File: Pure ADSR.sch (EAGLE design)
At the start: 42 parts, among them Q1 20MHz, U1 ATMEGA328P

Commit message: ADSR 2.1
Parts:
- removed BUT: PB6149L-5, INSTRUO:PB6149L-5
- removed IN, OUT: S_JACK, INSTRUO:S_JACK
- removed JP1: M05X2SHD, SparkFun-Connectors:M05X2SHD
- removed MODE: TOGGLE_ON_OFF_ON, INSTRUO:TOGGLE_ON_OFF_ON
- removed POT_A, POT_D, POT_R, POT_S: Q-POT, INSTRUO:Q-POT
- removed U$1: 2N3904, INSTRUO:TRANSISTOR_MMBT3904
- removed U$2: MCP4921, INSTRUO:MCP4921
- removed U$3: DUAL_OPAMP, INSTRUO:DUAL_OPAMP
- removed U$4: 7805, INSTRUO:V-REG
- removed U1: ATMEGA328P, SparkFun-DigitalIC:ATMEGA328_SMT
- added ATTACK, DECAY, RELEASE, SUSTAIN: 100k, GMSN:RESISTOR_VARIABLE9MM_POT
- added IC1: 78M05, GMSN:VOLTAGE_REG_POS05DT
- added IC2: OPAMP_DUALD, GMSN:OPAMP_DUALD
- added IC3: MCP4921, GMSN:DAC_SINGLE_12B_MCP4921
- added IC4: ATMEGA328P, GMSN:MICROPROCESSOR_ATMEGA328_SMT
- added MODESW: ON_OFF_ON, GMSN:SWITCH_TOGGLE_ON_OFF_ON
- added OUTPUT, TRIGATEIN: SOCKET_MONO_3.5MMPJ301M-12, GMSN:SOCKET_MONO_3.5MMPJ301M-12
- added POWER: HEADER2X5SHD, GMSN:HEADER2X5SHD
- added T1: MMBT2222A, GMSN:TRANSISTOR_NPNMMBT2222A
- added TRIGGER: PB6149L-5, GMSN:SWITCH_PUSHBUTTON_LED
- C1, C2, C6: device rcl:C-USC0805K -> GMSN:CAPACITOR-USC0805
- C10, C11, C12, C8, C9: value 0.1u -> 100nF; device rcl:C-USC0805K -> GMSN:CAPACITOR-USC0805
- C3: value 560p -> 10nF; device rcl:C-USC0805K -> GMSN:CAPACITOR-USC0805
- C4, C5, C7: device rcl:CPOL-US153CLV-0505 -> GMSN:CAPACITOR_POL-US153CLV-0505
- D1, D2: value (none) -> STTH102A; device adafruit:DIODESMA -> GMSN:DIODESMA
- ISP1: value AVRISP-6 -> HEADER2X3-6; device adafruit:AVRISP-6 -> GMSN:HEADER2X3-6
- Q1: device adafruit:CRYSTALHC49UP -> GMSN:CRYSTALHC49UP
- R1: value 47K -> 56k; device rcl:R-US_R0805 -> GMSN:RESISTOR_USR0805
- R10, R8: value 1K -> 1k; device rcl:R-US_R0805 -> GMSN:RESISTOR_USR0805
- R11, R12, R6: value 100K -> 100k; device rcl:R-US_R0805 -> GMSN:RESISTOR_USR0805
- R2: value 30K -> 30k; device rcl:R-US_R0805 -> GMSN:RESISTOR_USR0805
- R3: value 50K -> 56k; device rcl:R-US_R0805 -> GMSN:RESISTOR_USR0805
- R4, R7: device rcl:R-US_R0805 -> GMSN:RESISTOR_USR0805
- R5, R9: value 10K -> 10k; device rcl:R-US_R0805 -> GMSN:RESISTOR_USR0805
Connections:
- new net 5V: ATTACK.3, C10.1, C11.1, C12.1, DECAY.3, IC3.VDD, IC3.VREFA, IC4.AVCC, IC4.VCC@1, IC4.VCC@2, ISP1.VCC, R10.2, R5.2, R9.2, RELEASE.3, SUSTAIN.3
- net +12V: now also IC1.VI, IC2P.V+; no longer U$3G$3.+12V, U$4.IN
- net +5V: now also IC1.VO; no longer C10.1, C11.1, C12.1, ISP1.VCC, POT_A.3, POT_D.3, POT_R.3, POT_S.3, R10.2, R5.2, R9.2, U$2.VDD, U$2.VREFA, U$4.OUT, U1.AVCC, U1.VCC@1, U1.VCC@2
- net -12V: now also IC2P.V-; no longer U$3G$4.-12V
- net B_TRIG: now also IC4.PD3(INT1), IC4.PD4(XCK/T0), TRIGGERG$1.1, TRIGGERG$1.3; no longer BUTG$1.1, BUTG$1.3, U1.PD3(INT1), U1.PD4(XCK/T0)
- net CS: now also IC3.~CS, IC4.PB2(SS/OC1B); no longer U$2.~CS, U1.PB2(SS/OC1B)
- net GND: now also ATTACK.1, DECAY.1, IC1.GND, IC3.AVSS, IC3.~LDAC, IC4.AGND, IC4.GND@1, IC4.GND@2, OUTPUT.SLEEVE, POWER.3, POWER.4, POWER.5, POWER.6, POWER.7, POWER.8, RELEASE.1, SUSTAIN.1, T1.E, TRIGATEIN.SLEEVE, TRIGGERG$1.2, TRIGGERG$1.4; no longer BUTG$1.2, BUTG$1.4, IN.GND, JP1.3, JP1.4, JP1.5, JP1.6, JP1.7, JP1.8, OUT.GND, POT_A.1, POT_D.1, POT_R.1, POT_S.1, U$1.E, U$2.AVSS, U$2.~LDAC, U$4.GND, U1.AGND, U1.GND@1, U1.GND@2
- net MISO: now also IC4.PB4(MISO); no longer U1.PB4(MISO)
- net MOSI: now also IC3.SDI, IC4.PB3(MOSI/OC2); no longer U$2.SDI, U1.PB3(MOSI/OC2)
- net N$1: now also IC4.PB6(XTAL1/TOSC1); no longer U1.PB6(XTAL1/TOSC1)
- net N$10: now also POWER.1, POWER.2; no longer JP1.1, JP1.2
- net N$11: now also IC2A.OUT; no longer U$3G$1.OUT
- net N$12: now also MODESW.P; no longer MODE.P
- net N$15: now also T1.B; no longer U$1.B
- net N$18: now also TRIGATEIN.TIP; no longer IN.TIP
- net N$2: now also IC4.PB7(XTAL2/TOSC2); no longer U1.PB7(XTAL2/TOSC2)
- net N$3: now also IC3.VOUTA; no longer U$2.VOUTA
- net N$4: now also IC2A.+IN, IC2B.+IN; no longer U$3G$1.+IN, U$3G$2.+IN
- net N$5: now also IC2A.-IN; no longer U$3G$1.-IN
- net N$6: now also OUTPUT.TIP; no longer OUT.TIP
- net N$7: now also IC2B.-IN, IC2B.OUT, TRIGGERG$2.A; no longer BUTG$2.A, U$3G$2.-IN, U$3G$2.OUT
- net N$8: now also TRIGGERG$2.C; no longer BUTG$2.C
- net N$9: now also POWER.10, POWER.9; no longer JP1.10, JP1.9
- net POT_A: now also ATTACK.2, IC4.PC3(ADC3); no longer POT_A.2, U1.PC3(ADC3)
- net POT_D: now also DECAY.2, IC4.PC2(ADC2); no longer POT_D.2, U1.PC2(ADC2)
- net POT_R: now also IC4.PC0(ADC0), RELEASE.2; no longer POT_R.2, U1.PC0(ADC0)
- net POT_S: now also IC4.PC1(ADC1), SUSTAIN.2; no longer POT_S.2, U1.PC1(ADC1)
- net RST: now also IC4.PC6(/RESET); no longer U1.PC6(/RESET)
- net SCK: now also IC3.SCK, IC4.PB5(SCK); no longer U$2.SCK, U1.PB5(SCK)
- net T1: now also IC4.PD6(AIN0), MODESW.S; no longer MODE.S, U1.PD6(AIN0)
- net T2: now also IC4.PD7(AIN1), MODESW.O; no longer MODE.O, U1.PD7(AIN1)
- net TRIG: now also IC4.PD2(INT0), IC4.PD5(T1), T1.C; no longer U$1.C, U1.PD2(INT0), U1.PD5(T1)

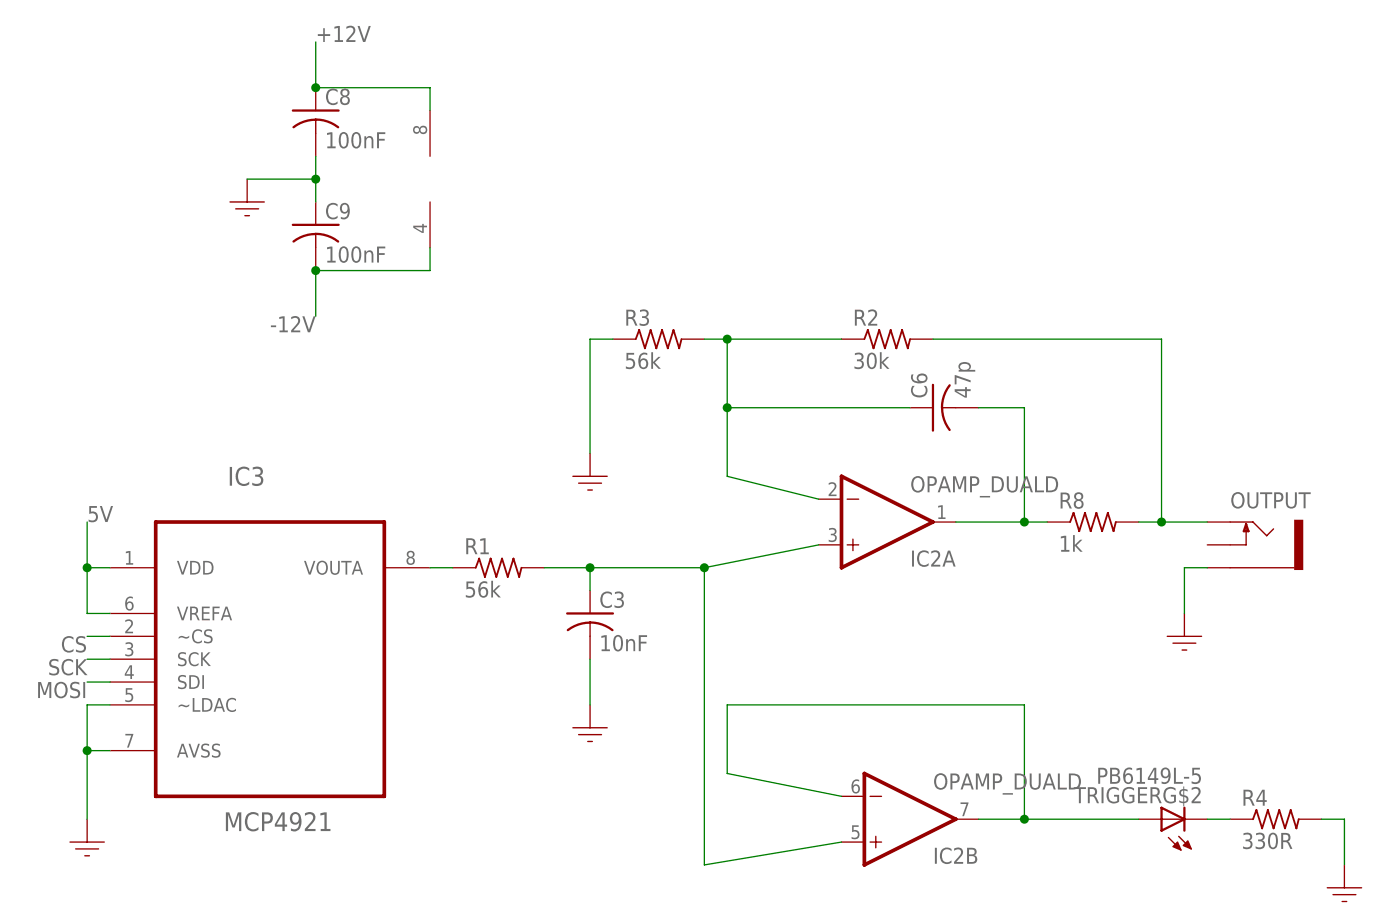
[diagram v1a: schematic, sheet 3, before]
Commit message: ADSR 2.2
ADSR Updated to V2.2 14/4/21

Library updated to include 3D models.
Traces rerouted.
DAC output filter remodelled.
Power replaced so 5V comes from power supply rather than 12V, in line with low noise techniques.
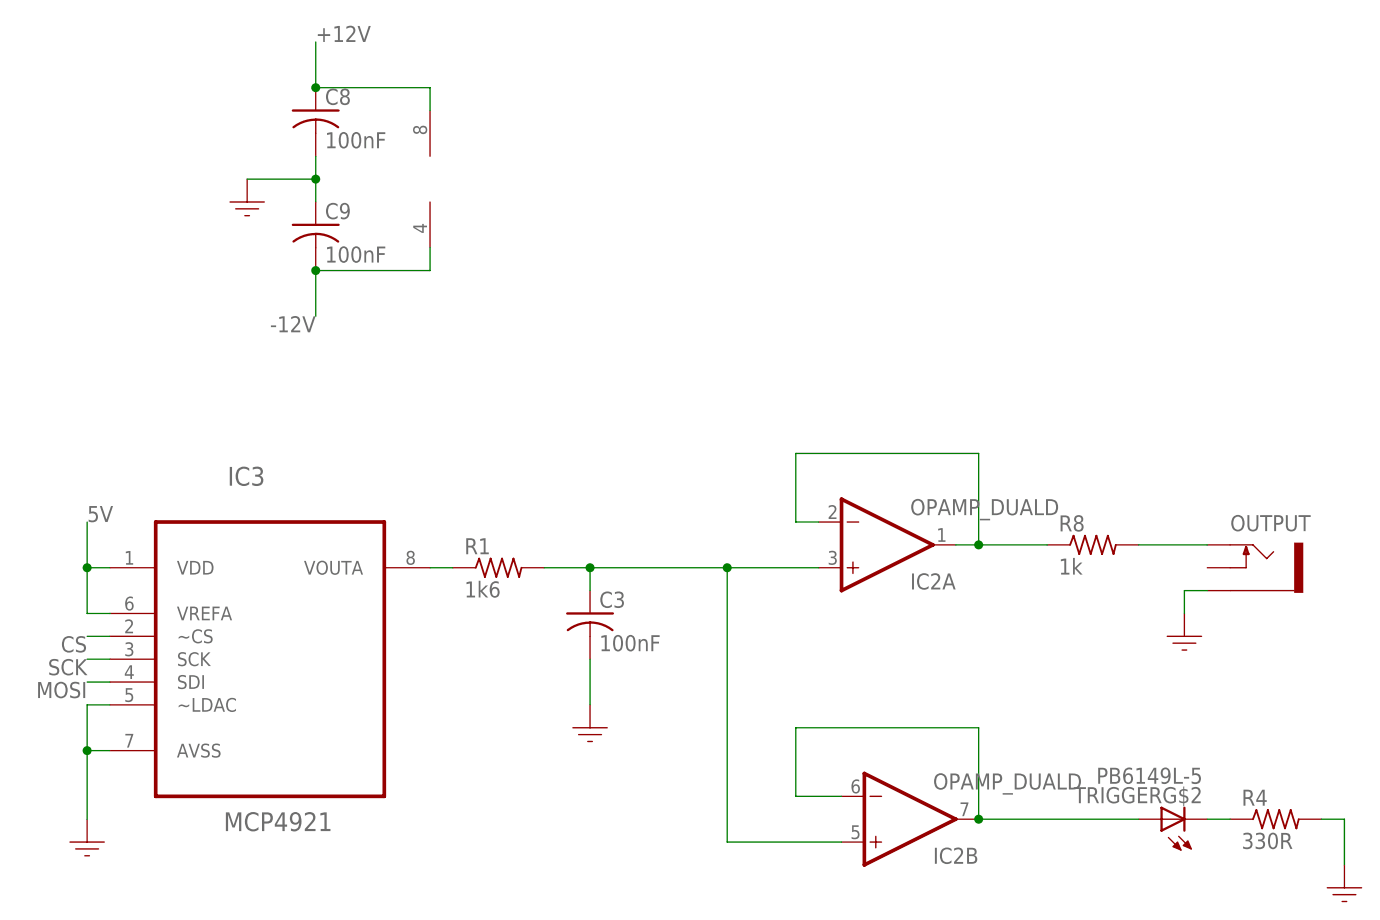
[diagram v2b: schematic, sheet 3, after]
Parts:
- removed C6: 47p, GMSN:CAPACITOR-USC0805
- removed IC1: 78M05, GMSN:VOLTAGE_REG_POS05DT
- removed POWER: HEADER2X5SHD, GMSN:HEADER2X5SHD
- removed R2: 30k, GMSN:RESISTOR_USR0805
- removed R3: 56k, GMSN:RESISTOR_USR0805
- added JP1: HEADER2X8, GMSN:HEADER2X8
- C3: value 10nF -> 100nF
- MODESW: device GMSN:SWITCH_TOGGLE_ON_OFF_ON -> GMSN:SWITCH_TOGGLE_SPDT
- R1: value 56k -> 1k6
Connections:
- removed net +5V: C7.+, IC1.VO
- removed net N$10: D2.C, POWER.1, POWER.2
- removed net N$11: C6.2, IC2A.OUT, R8.1
- removed net N$6: OUTPUT.TIP, R2.2, R8.2
- new net N$13: D2.C, JP1.1, JP1.2
- new net N$19: D1.A, JP1.10, JP1.9
- net +12V: no longer IC1.VI
- net 5V: now also C7.+, JP1.11, JP1.12
- net B_TRIG: now also IC4.3(INT1), IC4.4; no longer IC4.PD3(INT1), IC4.PD4(XCK/T0)
- net CS: now also IC4.10(OCIB); no longer IC4.PB2(SS/OC1B)
- net GND: now also JP1.3, JP1.4, JP1.5, JP1.6, JP1.7, JP1.8; no longer IC1.GND, POWER.3, POWER.4, POWER.5, POWER.6, POWER.7, POWER.8, R3.1
- net MISO: now also IC4.12(MISO); no longer IC4.PB4(MISO)
- net MOSI: now also IC4.11(MOSI); no longer IC4.PB3(MOSI/OC2)
- net N$5: now also IC2A.OUT, R8.1; no longer C6.1, R2.1, R3.2
- net N$9: now also OUTPUT.TIP, R8.2; no longer D1.A, POWER.10, POWER.9
- net POT_A: now also IC4.A3; no longer IC4.PC3(ADC3)
- net POT_D: now also IC4.A2; no longer IC4.PC2(ADC2)
- net POT_R: now also IC4.A0; no longer IC4.PC0(ADC0)
- net POT_S: now also IC4.A1; no longer IC4.PC1(ADC1)
- net SCK: now also IC4.13(SCK); no longer IC4.PB5(SCK)
- net T1: now also IC4.6; no longer IC4.PD6(AIN0)
- net T2: now also IC4.7; no longer IC4.PD7(AIN1)
- net TRIG: now also IC4.2(INT0), IC4.5; no longer IC4.PD2(INT0), IC4.PD5(T1)
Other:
- moved on the sheet: IC2A, OUTPUT, R8

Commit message: Reinstall
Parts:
- T1: value MMBT2222A -> 2N3904
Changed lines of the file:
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@@
 <part name="RELEASE" library="GMSN" library_urn="urn:adsk.eagle:library:27425118" deviceset="RESISTOR_VARIABLE" device="9MM_POT" package3d_urn="urn:adsk.eagle:package:27425927/2" value="100k"/>
 <part name="GND9" library="GMSN" library_urn="urn:adsk.eagle:library:27425118" deviceset="GND" device=""/>
-<part name="T1" library="GMSN" library_urn="urn:adsk.eagle:library:27425118" deviceset="TRANSISTOR_NPN" device="MMBT2222A" package3d_urn="urn:adsk.eagle:package:27426301/1" value="MMBT2222A"/>
+<part name="T1" library="GMSN" library_urn="urn:adsk.eagle:library:27425118" deviceset="TRANSISTOR_NPN" device="MMBT2222A" package3d_urn="urn:adsk.eagle:package:27426301/1" value="2N3904"/>
 <part name="GND10" library="GMSN" library_urn="urn:adsk.eagle:library:27425118" deviceset="GND" device=""/>
 <part name="R5" library="GMSN" library_urn="urn:adsk.eagle:library:27425118" deviceset="RESISTOR_US" device="R0805" package3d_urn="urn:adsk.eagle:package:27425978/1" value="10k"/>
